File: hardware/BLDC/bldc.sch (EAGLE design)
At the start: 78 parts, among them J1 PWR_2_XT30PW-M, J2 LINEAR_3_JST_PH_RA, J3 LINEAR_8_JST_PH_RA, U1 MA702, U10 MCP2542FD, U11 LDFM33PUR, U2 DRV8323RS, U3 TPN7R006PL, U4 TPN7R006PL, U5 TPN7R006PL, U6 TPN7R006PL, U7 TPN7R006PL, U8 TPN7R006PL, U9 STM32G4_UFQFPN48_T1, X1 CRYSTAL_NX2016SA-24MHZ-EXS00A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

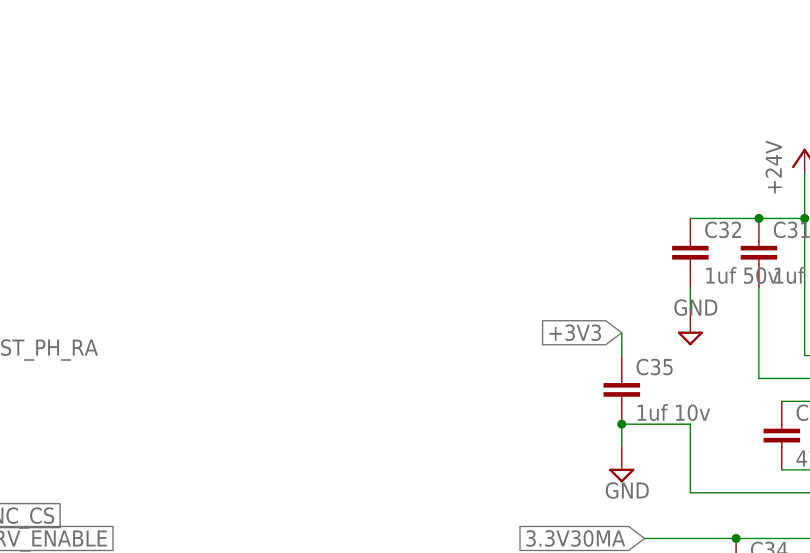
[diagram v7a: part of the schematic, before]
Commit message: Added status LEDs
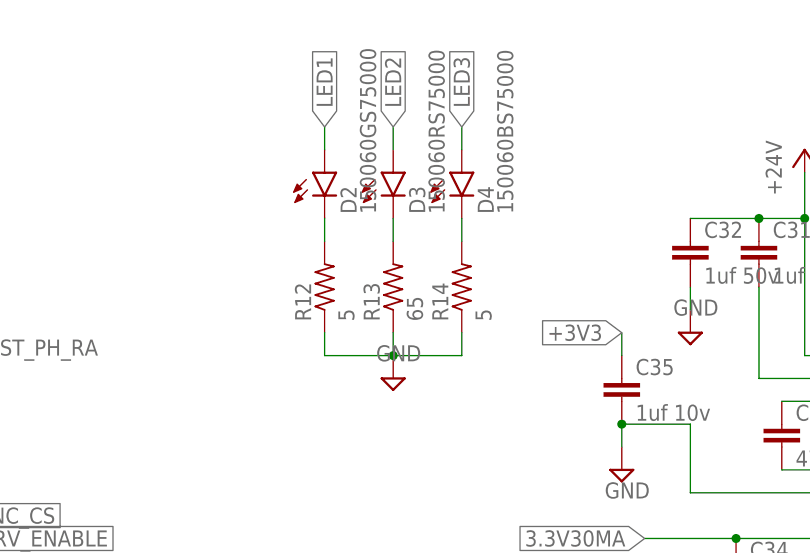
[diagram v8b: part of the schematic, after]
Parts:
- added D2: 150060GS75000, _T_rcl:LED_0603
- added D3: 150060RS75000, _T_rcl:LED_0603
- added D4: 150060BS75000, _T_rcl:LED_0603
- added R12, R14: 5, _T_rcl:R0402
- added R13: 65, _T_rcl:R0402
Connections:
- new net N$10: D2.C, R12.2
- new net N$4: D4.C, R14.2
- new net N$7: D3.C, R13.2
- net GND: now also R12.1, R13.1, R14.1
- net LED1: now also D2.A
- net LED2: now also D3.A
- net LED3: now also D4.A
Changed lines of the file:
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@@
 <part name="+3V3" library="_T_power" library_urn="urn:adsk.eagle:library:19572085" deviceset="+3V3" device=""/>
 <part name="+24V8" library="_T_power" library_urn="urn:adsk.eagle:library:19572085" deviceset="+24V" device=""/>
+<part name="D2" library="_T_rcl" library_urn="urn:adsk.eagle:library:19571919" deviceset="LED" device="_0603" package3d_urn="urn:adsk.eagle:package:19545722/3" value="150060GS75000"/>
+<part name="D3" library="_T_rcl" library_urn="urn:adsk.eagle:library:19571919" deviceset="LED" device="_0603" package3d_urn="urn:adsk.eagle:package:19545722/3" value="150060RS75000"/>
+<part name="D4" library="_T_rcl" library_urn="urn:adsk.eagle:library:19571919" deviceset="LED" device="_0603" package3d_urn="urn:adsk.eagle:package:19545722/3" value="150060BS75000"/>
+<part name="R12" library="_T_rcl" library_urn="urn:adsk.eagle:library:19571919" deviceset="R" device="0402" package3d_urn="urn:adsk.eagle:package:19572014/3" value="5"/>
+<part name="R13" library="_T_rcl" library_urn="urn:adsk.eagle:library:19571919" deviceset="R" device="0402" package3d_urn="urn:adsk.eagle:package:19572014/3" value="65"/>
+<part name="R14" library="_T_rcl" library_urn="urn:adsk.eagle:library:19571919" deviceset="R" device="0402" package3d_urn="urn:adsk.eagle:package:19572014/3" value="5"/>
+<part name="GND28" library="_T_power" library_urn="urn:adsk.eagle:library:19572085" deviceset="GND" device=""/>
 </parts>
 <sheets>
@@
 <instance part="+24V8" gate="G$1" x="147.32" y="149.86" smashed="yes">
 <attribute name="VALUE" x="144.78" y="144.78" size="1.778" layer="96" rot="R90"/>
+</instance>
+<instance part="D2" gate="G$1" x="45.72" y="165.1" smashed="yes">
+<attribute name="NAME" x="49.276" y="160.528" size="1.778" layer="95" rot="R90"/>
+<attribute name="VALUE" x="51.435" y="160.528" size="1.778" layer="96" rot="R90"/>
+</instance>
+<instance part="D3" gate="G$1" x="53.34" y="165.1" smashed="yes">
+<attribute name="NAME" x="56.896" y="160.528" size="1.778" layer="95" rot="R90"/>
+<attribute name="VALUE" x="59.055" y="160.528" size="1.778" layer="96" rot="R90"/>
+</instance>
+<instance part="D4" gate="G$1" x="60.96" y="165.1" smashed="yes">
+<attribute name="NAME" x="64.516" y="160.528" size="1.778" layer="95" rot="R90"/>
+<attribute name="VALUE" x="66.675" y="160.528" size="1.778" layer="96" rot="R90"/>
+</instance>
+<instance part="R12" gate="G$1" x="45.72" y="152.4" smashed="yes" rot="R90">
+<attribute name="NAME" x="44.2214" y="148.59" size="1.778" layer="95" rot="R90"/>
+<attribute name="VALUE" x="49.022" y="148.59" size="1.778" layer="96" rot="R90"/>
+</instance>
+<instance part="R13" gate="G$1" x="53.34" y="152.4" smashed="yes" rot="R90">
+<attribute name="NAME" x="51.8414" y="148.59" size="1.778" layer="95" rot="R90"/>
+<attribute name="VALUE" x="56.642" y="148.59" size="1.778" layer="96" rot="R90"/>
+</instance>
+<instance part="R14" gate="G$1" x="60.96" y="152.4" smashed="yes" rot="R90">
+<attribute name="NAME" x="59.4614" y="148.59" size="1.778" layer="95" rot="R90"/>
+<attribute name="VALUE" x="64.262" y="148.59" size="1.778" layer="96" rot="R90"/>
+</instance>
+<instance part="GND28" gate="G$1" x="53.34" y="142.24" smashed="yes">
+<attribute name="VALUE" x="51.435" y="144.145" size="1.778" layer="96"/>
 </instance>
 </instances>
@@
 <label x="-48.26" y="60.96" size="1.778" layer="95" rot="R180" xref="yes"/>
 </segment>
+<segment>
+<pinref part="D2" gate="G$1" pin="A"/>
+<wire x1="45.72" y1="167.64" x2="45.72" y2="170.18" width="0.1524" layer="91"/>
+<label x="45.72" y="170.18" size="1.778" layer="95" rot="R90" xref="yes"/>
+</segment>
 </net>
 <net name="LED2" class="0">
@@
 <label x="-48.26" y="68.58" size="1.778" layer="95" rot="R180" xref="yes"/>
 </segment>
+<segment>
+<pinref part="D3" gate="G$1" pin="A"/>
+<wire x1="53.34" y1="167.64" x2="53.34" y2="170.18" width="0.1524" layer="91"/>
+<label x="53.34" y="170.18" size="1.778" layer="95" rot="R90" xref="yes"/>
+</segment>
 </net>
 <net name="LED3" class="0">
@@
 <wire x1="-43.18" y1="66.04" x2="-48.26" y2="66.04" width="0.1524" layer="91"/>
 <label x="-48.26" y="66.04" size="1.778" layer="95" rot="R180" xref="yes"/>
+</segment>
+<segment>
+<pinref part="D4" gate="G$1" pin="A"/>
+<wire x1="60.96" y1="167.64" x2="60.96" y2="170.18" width="0.1524" layer="91"/>
+<label x="60.96" y="170.18" size="1.778" layer="95" rot="R90" xref="yes"/>
 </segment>
 </net>
@@
 <wire x1="160.02" y1="60.96" x2="160.02" y2="63.5" width="0.1524" layer="91"/>
 </segment>
+<segment>
+<pinref part="R14" gate="G$1" pin="1"/>
+<pinref part="GND28" gate="G$1" pin="GND"/>
+<wire x1="60.96" y1="147.32" x2="60.96" y2="144.78" width="0.1524" layer="91"/>
+<wire x1="60.96" y1="144.78" x2="53.34" y2="144.78" width="0.1524" layer="91"/>
+<pinref part="R12" gate="G$1" pin="1"/>
+<wire x1="45.72" y1="147.32" x2="45.72" y2="144.78" width="0.1524" layer="91"/>
+<wire x1="45.72" y1="144.78" x2="53.34" y2="144.78" width="0.1524" layer="91"/>
+<junction x="53.34" y="144.78"/>
+<pinref part="R13" gate="G$1" pin="1"/>
+<wire x1="53.34" y1="147.32" x2="53.34" y2="144.78" width="0.1524" layer="91"/>
+</segment>
 </net>
 <net name="+24V" class="2">
@@
 </segment>
 </net>
+<net name="N$4" class="0">
+<segment>
+<pinref part="D4" gate="G$1" pin="C"/>
+<pinref part="R14" gate="G$1" pin="2"/>
+<wire x1="60.96" y1="160.02" x2="60.96" y2="157.48" width="0.1524" layer="91"/>
+</segment>
+</net>
+<net name="N$7" class="0">
+<segment>
+<pinref part="D3" gate="G$1" pin="C"/>
+<pinref part="R13" gate="G$1" pin="2"/>
+<wire x1="53.34" y1="160.02" x2="53.34" y2="157.48" width="0.1524" layer="91"/>
+</segment>
+</net>
+<net name="N$10" class="0">
+<segment>
+<pinref part="D2" gate="G$1" pin="C"/>
+<pinref part="R12" gate="G$1" pin="2"/>
+<wire x1="45.72" y1="160.02" x2="45.72" y2="157.48" width="0.1524" layer="91"/>
+</segment>
+</net>
